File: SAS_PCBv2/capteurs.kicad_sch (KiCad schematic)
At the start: 0 parts

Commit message: bmp280 + LogicLevelShifterPN I2C
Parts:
- added C1, C2: 100nF, symbol Device:C
- added J1: BMP280, symbol Connector_Generic:Conn_01x06
- added R1: 10k, symbol Device:R
- added U1: TXS0102DCUT, SAS_PCBv2_footprint:SOP50P310X90-8N, symbol SAS_PCBv2_symbol:TXS0102DCUT
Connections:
- new net +3V3: C2.2, J1.1 (Vcc), R1.1, U1.3 (VCCA), U1.6 (OE)
- new net +5V: C1.2, U1.7 (VCCB)
- new net GND: C1.1, C2.1, J1.2 (Pin_2), J1.6 (Pin_6), R1.2, U1.2 (GND)
- new net I2C 3V3 SCL: J1.3 (Pin_3)
- new net I2C 3V3 SDA: J1.4 (Pin_4)
- new net I2C_3V3_SCL: U1.5 (A1)
- new net I2C_3V3_SDA: U1.4 (A2)
- new net I2C_5V_SCL: U1.8 (B1)
- new net I2C_5V_SDA: U1.1 (B2)
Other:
- note added: "Barometre BMP280"
- note added: "Current draw 100mA"
- note added: "Current draw 40uA"
- note added: "Enable active high"
- note added: "I2C address SDO_low = 0x76"
- note added: "Logic level shifter PN"

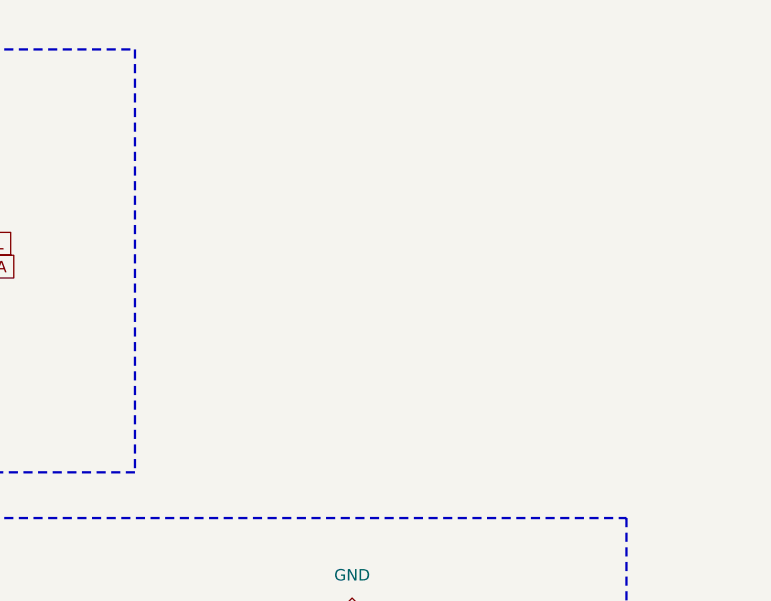
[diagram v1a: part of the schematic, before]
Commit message: Radio et GPS fait selon les datasheets normalement
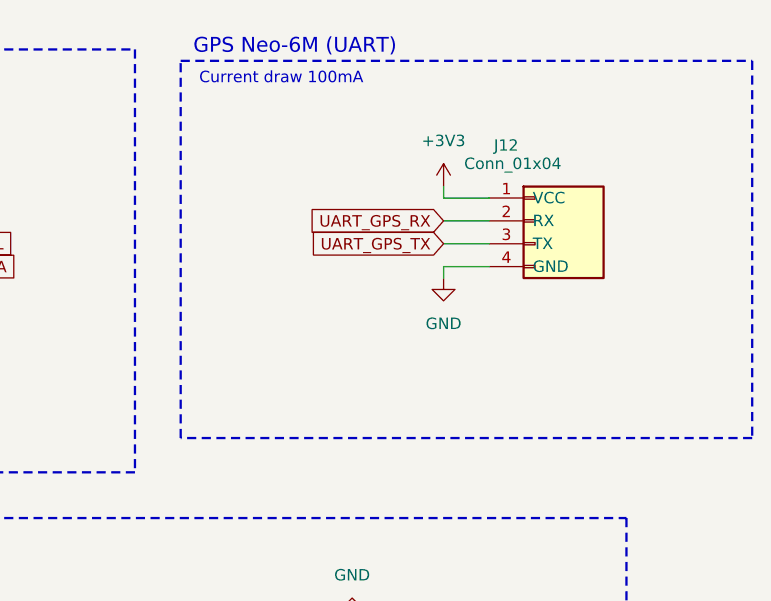
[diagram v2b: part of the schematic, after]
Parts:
- added J12: Conn_01x04, symbol Connector_Generic:Conn_01x04
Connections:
- net +3V3: now also J12.1 (VCC)
- net GND: now also J12.4 (GND)
- new net UART_GPS_RX: J12.2 (RX)
- new net UART_GPS_TX: J12.3 (TX)
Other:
- note added: "GPS Neo-6M (UART)"

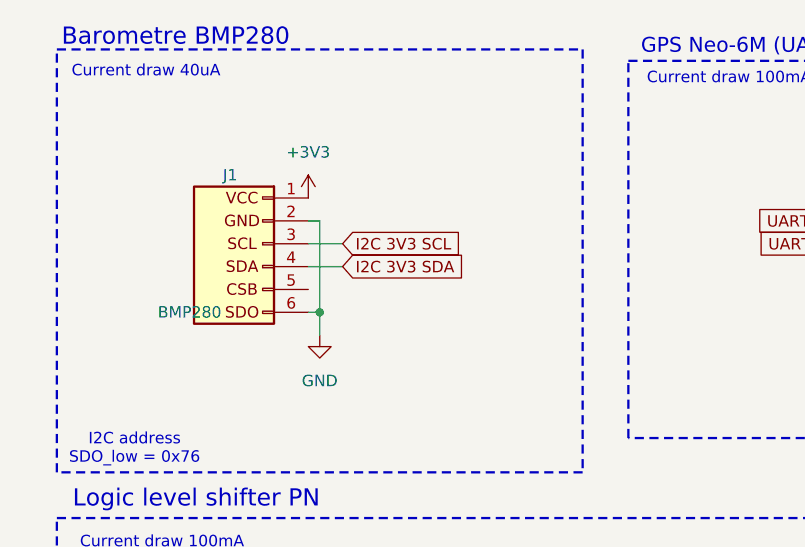
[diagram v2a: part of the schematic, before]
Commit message: schematic sans error et le debut de pcb
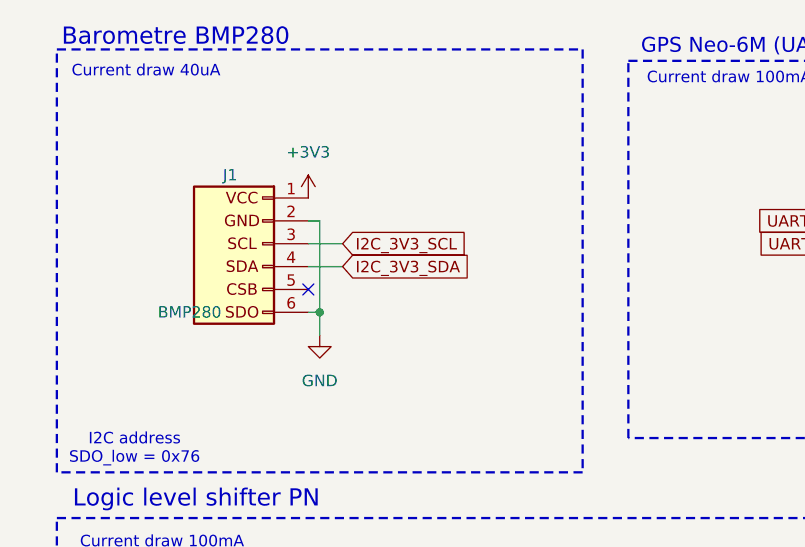
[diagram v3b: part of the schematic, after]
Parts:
- C1, C2: footprint (none) -> Capacitor_THT:C_Disc_D5.0mm_W2.5mm_P2.50mm
- J1: footprint (none) -> Connector_PinHeader_2.54mm:PinHeader_1x06_P2.54mm_Vertical
- J12: footprint (none) -> Connector_PinHeader_2.54mm:PinHeader_1x04_P2.54mm_Vertical
- R1: footprint (none) -> Resistor_THT:R_Axial_DIN0207_L6.3mm_D2.5mm_P10.16mm_Horizontal
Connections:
- net I2C 3V3 SCL is gone; now on net I2C_3V3_SCL: J1.3 (Pin_3)
- net I2C 3V3 SDA is gone; now on net I2C_3V3_SDA: J1.4 (Pin_4)
- no-connect marks 0 -> 1
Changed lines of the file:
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@@
 		(color 0 0 0 0)
 	)
+	(no_connect
+		(at 43.18 44.45)
+	)
 	(wire
 		(pts
@@
 		)
 	)
-	(global_label "I2C 3V3 SDA"
+	(global_label "I2C_3V3_SDA"
 		(shape input)
 		(at 46.99 41.91 0)
@@
 		)
 		(property "Intersheetrefs" "${INTERSHEET_REFS}"
-			(at 62.0099 41.91 0)
+			(at 62.0704 41.91 0)
 			(effects
 				(font
@@
 		)
 	)
-	(global_label "I2C 3V3 SCL"
+	(global_label "I2C_3V3_SCL"
 		(shape input)
 		(at 46.99 39.37 0)
@@
 			)
 		)
-		(property "Footprint" ""
+		(property "Footprint" "Connector_PinHeader_2.54mm:PinHeader_1x04_P2.54mm_Vertical"
 			(at 118.11 36.83 0)
 			(effects
@@
 			)
 		)
-		(property "Footprint" ""
+		(property "Footprint" "Capacitor_THT:C_Disc_D5.0mm_W2.5mm_P2.50mm"
 			(at 53.0352 91.44 0)
 			(effects
@@
 			)
 		)
-		(property "Footprint" ""
+		(property "Footprint" "Connector_PinHeader_2.54mm:PinHeader_1x06_P2.54mm_Vertical"
 			(at 38.1 39.37 0)
 			(effects
@@
 			)
 		)
-		(property "Footprint" ""
+		(property "Footprint" "Resistor_THT:R_Axial_DIN0207_L6.3mm_D2.5mm_P10.16mm_Horizontal"
 			(at 50.292 130.81 90)
 			(effects
@@
 			)
 		)
-		(property "Footprint" ""
+		(property "Footprint" "Capacitor_THT:C_Disc_D5.0mm_W2.5mm_P2.50mm"
 			(at 98.7552 90.17 0)
 			(effects

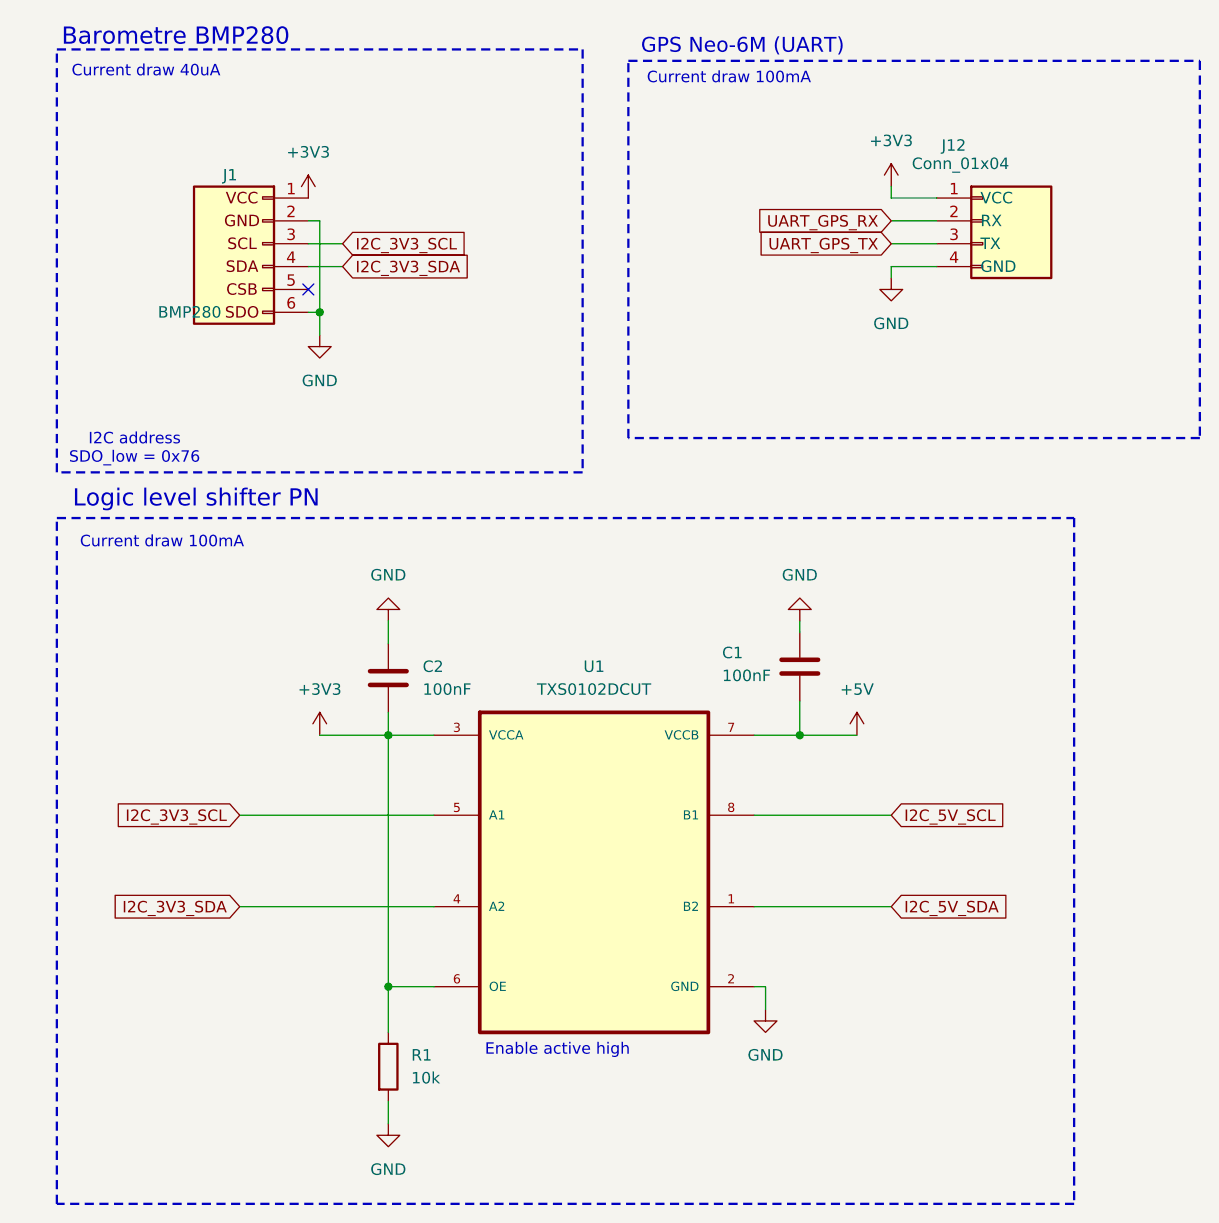
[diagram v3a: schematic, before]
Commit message: Switch USB/PCB, connections Power, spam condensateurs, resistance pull-up
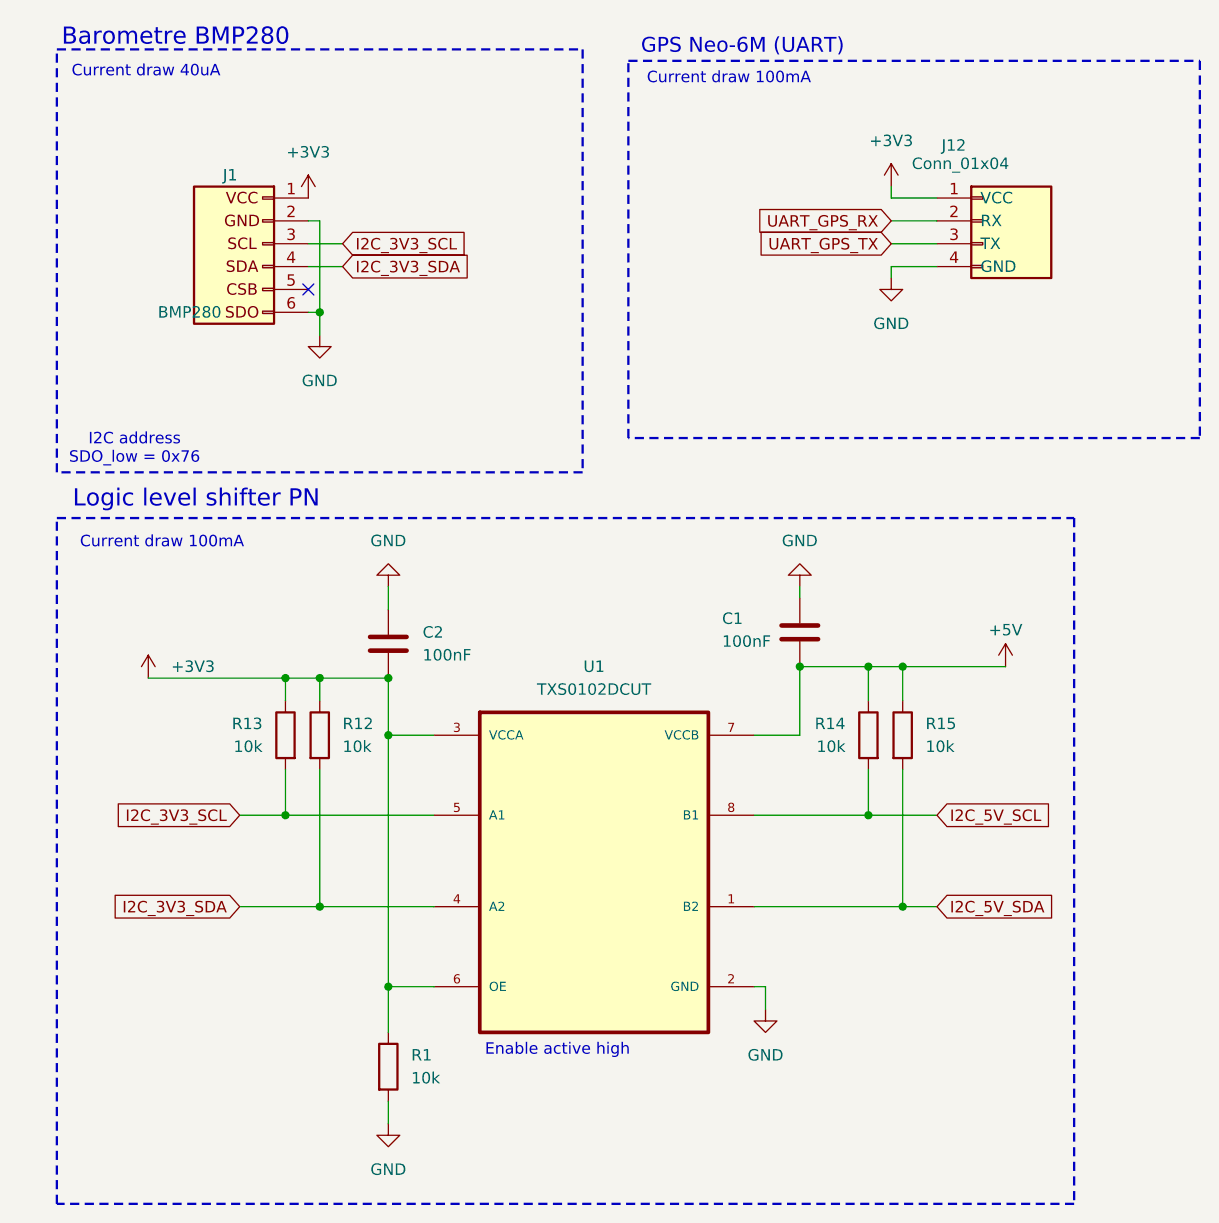
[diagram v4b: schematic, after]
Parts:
- added R12, R13, R14, R15: 10k, Resistor_THT:R_Axial_DIN0207_L6.3mm_D2.5mm_P10.16mm_Horizontal, symbol Device:R
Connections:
- net +3V3: now also R12.1, R13.1
- net +5V: now also R14.1, R15.1
- net I2C_3V3_SCL: now also R13.2
- net I2C_3V3_SDA: now also R12.2
- net I2C_5V_SCL: now also R14.2
- net I2C_5V_SDA: now also R15.2
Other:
- moved on the sheet: C1, C2

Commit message: LDO du service, Logic level shifter custom
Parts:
- removed C1, C2: 100nF, Capacitor_THT:C_Disc_D5.0mm_W2.5mm_P2.50mm, symbol Device:C
- removed R15: 10k, Resistor_THT:R_Axial_DIN0207_L6.3mm_D2.5mm_P10.16mm_Horizontal, symbol Device:R
- removed U1: TXS0102DCUT, SAS_PCBv2_footprint:SOP50P310X90-8N, symbol SAS_PCBv2_symbol:TXS0102DCUT
- added Q4, Q5: BS170, Package_TO_SOT_THT:TO-92_Inline, symbol Transistor_FET:BS170
- R1, R12, R13, R14: footprint Resistor_THT:R_Axial_DIN0207_L6.3mm_D2.5mm_P10.16mm_Horizontal -> (none)
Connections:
- net +3V3: now also Q4.2 (G), Q5.2 (G); no longer R12.1
- net +5V: now also R12.1
- net GND: no longer R1.2
- net I2C_3V3_SCL: now also R1.2, Q4.3 (S); no longer R13.2
- net I2C_3V3_SDA: now also R13.2, Q5.3 (S); no longer R12.2
- net I2C_5V_SCL: now also R12.2, Q4.1 (D); no longer R14.2
- net I2C_5V_SDA: now also R14.2, Q5.1 (D)
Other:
- note removed: "Enable active high"
